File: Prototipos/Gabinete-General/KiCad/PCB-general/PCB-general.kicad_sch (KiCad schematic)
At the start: 14 parts, among them J1 Conn_01x02, J2 Conn_01x02, J3 TFT Display, J4 PCIe X4, SW1 RotaryEncoder_Switch, U1 ESP32-S3-DevKitC, U2 LM7805_TO220

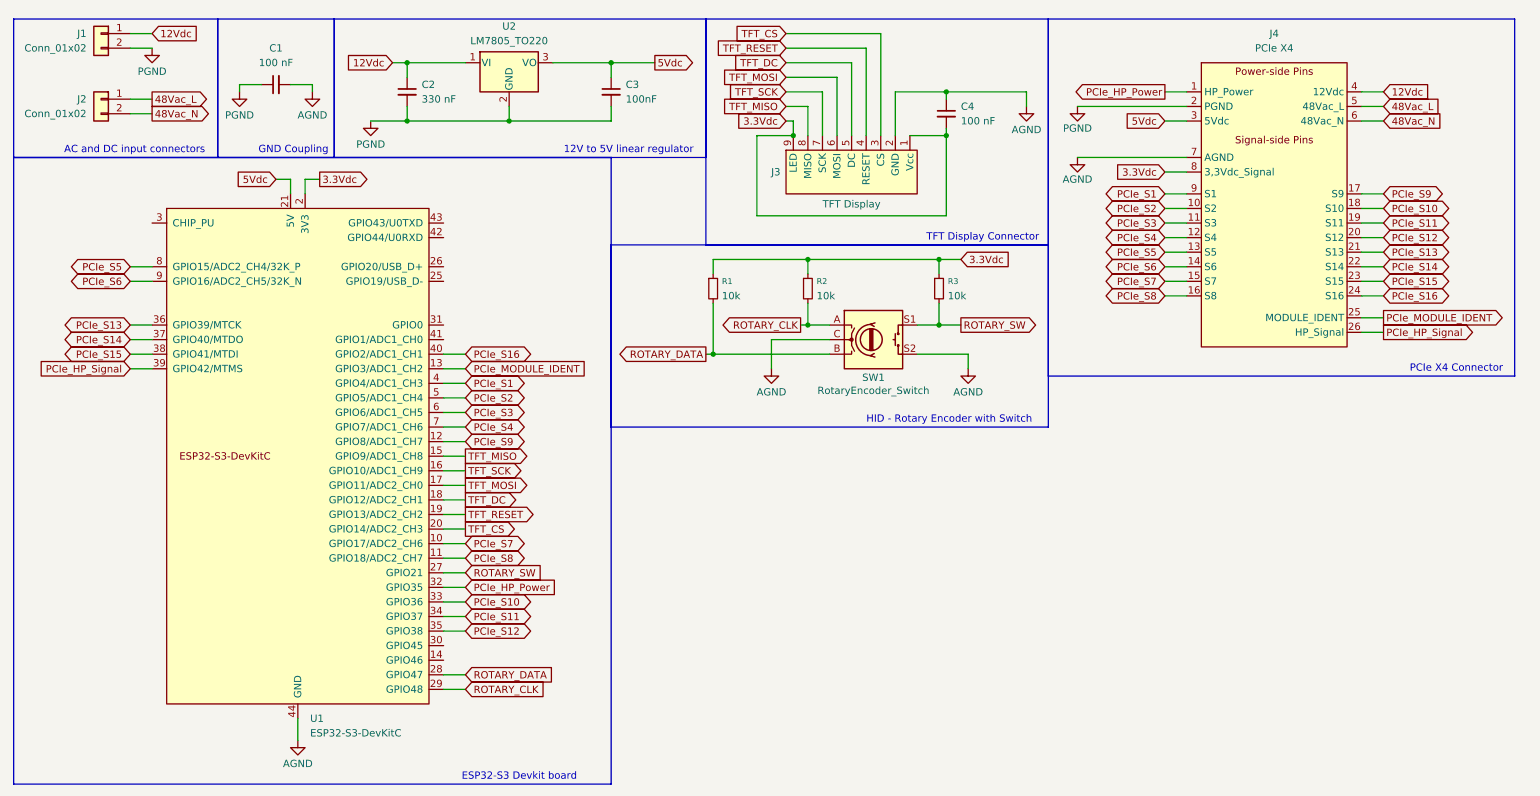
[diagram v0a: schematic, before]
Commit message: Rediseñar PCB gabinete central
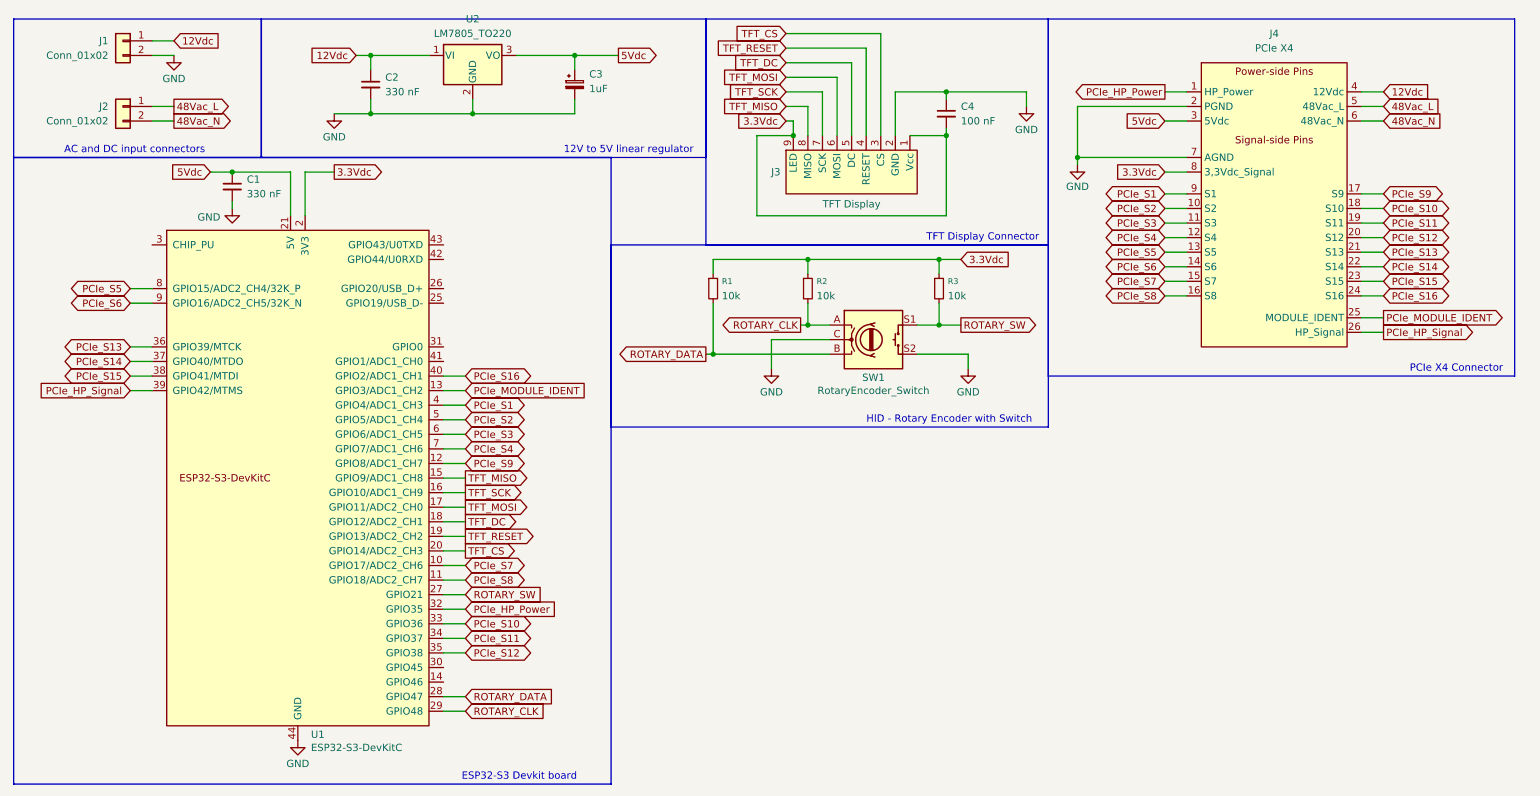
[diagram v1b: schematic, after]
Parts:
- C1: value 100 nF -> 330 nF
- C3: value 100nF -> 1uF; symbol Device:C_Small -> Device:C_Polarized_Small
- J4: footprint Proyecto_Final:PCIE_x4_Gabinete_NSH -> ProyectoFinal:PCIE_x4_Gabinete_NSH
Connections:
- net 5Vdc: now also C1.1
- net AGND renamed GND
- net GND: now also C2.2, C3.2, J1.2 (Pin_2), J4.2 (PGND), U2.2 (GND)
- removed net PGND: C1.1, C2.2, C3.2, J1.2 (Pin_2), J4.2 (PGND), U2.2 (GND)
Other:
- note removed: "GND Coupling"
- moved on the sheet: C2, J1, J2, U1, U2

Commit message: Agrandar tamaño pad vias
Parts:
- C3: footprint Capacitor_THT:C_Disc_D3.0mm_W2.0mm_P2.50mm -> Capacitor_THT:C_Radial_D4.0mm_H7.0mm_P1.50mm
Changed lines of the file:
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@@
 			)
 		)
-		(property "Footprint" "Capacitor_THT:C_Disc_D3.0mm_W2.0mm_P2.50mm"
+		(property "Footprint" "Capacitor_THT:C_Radial_D4.0mm_H7.0mm_P1.50mm"
 			(at 115.57 44.45 0)
 			(effects
